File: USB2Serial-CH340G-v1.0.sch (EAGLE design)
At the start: 23 parts, among them CN2 47346-0001, IC2 AMS1117-3.3, Q1 12MHz, U1 CH340G

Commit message: Fix some names
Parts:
- CN1: value (none) -> UART
- renumbered IC2 to IC1, J1 to CN1
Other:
- note added: "(c) Andriy Golovnya"
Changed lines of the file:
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@@
 <part name="C5" library="rcl" library_urn="urn:adsk.eagle:library:334" deviceset="C-EU" device="C0402" package3d_urn="urn:adsk.eagle:package:23626/2" value="100nF"/>
 <part name="C6" library="rcl" library_urn="urn:adsk.eagle:library:334" deviceset="C-EU" device="C0402" package3d_urn="urn:adsk.eagle:package:23626/2" value="100nF"/>
-<part name="IC2" library="v-reg" library_urn="urn:adsk.eagle:library:409" deviceset="LD117A?*" device="S" package3d_urn="urn:adsk.eagle:package:30370/1" technology="33TR" value="AMS1117-3.3"/>
+<part name="IC1" library="v-reg" library_urn="urn:adsk.eagle:library:409" deviceset="LD117A?*" device="S" package3d_urn="urn:adsk.eagle:package:30370/1" technology="33TR" value="AMS1117-3.3"/>
 <part name="SUPPLY2" library="SparkFun-PowerSymbols" library_urn="urn:adsk.eagle:library:530" deviceset="5V" device=""/>
 <part name="SUPPLY3" library="SparkFun-PowerSymbols" library_urn="urn:adsk.eagle:library:530" deviceset="3.3V" device=""/>
@@
 <part name="GND5" library="SparkFun-PowerSymbols" library_urn="urn:adsk.eagle:library:530" deviceset="GND" device=""/>
 <part name="FRAME1" library="frames" library_urn="urn:adsk.eagle:library:229" deviceset="DINA4_L" device=""/>
-<part name="J1" library="SparkFun-Connectors" library_urn="urn:adsk.eagle:library:513" deviceset="CONN_06" device="NO_SILK_FEMALE_PTH" package3d_urn="urn:adsk.eagle:package:38130/1"/>
+<part name="CN1" library="SparkFun-Connectors" library_urn="urn:adsk.eagle:library:513" deviceset="CONN_06" device="NO_SILK_FEMALE_PTH" package3d_urn="urn:adsk.eagle:package:38130/1" value="UART"/>
 <part name="GND1" library="SparkFun-PowerSymbols" library_urn="urn:adsk.eagle:library:530" deviceset="GND" device=""/>
 <part name="SUPPLY1" library="SparkFun-PowerSymbols" library_urn="urn:adsk.eagle:library:530" deviceset="5V" device=""/>
@@
 <text x="111.76" y="144.78" size="2.54" layer="94">3.3V generation</text>
 <text x="40.64" y="144.78" size="2.54" layer="94">LED indicators</text>
-<text x="177.8" y="144.78" size="2.54" layer="94">UART connector and VCC selection</text>
+<text x="175.26" y="144.78" size="2.54" layer="94">UART connector and VCC selection</text>
+<text x="165.1" y="27.94" size="2.54" layer="94">(c) Andriy Golovnya</text>
 </plain>
 <instances>
@@
 <attribute name="VALUE" x="138.684" y="117.221" size="1.778" layer="96"/>
 </instance>
-<instance part="IC2" gate="G$1" x="119.38" y="129.54" smashed="yes">
+<instance part="IC1" gate="G$1" x="119.38" y="129.54" smashed="yes">
 <attribute name="NAME" x="111.76" y="134.62" size="1.778" layer="95"/>
 <attribute name="VALUE" x="119.38" y="134.62" size="1.778" layer="96"/>
@@
 <attribute name="DRAWING_NAME" x="180.34" y="19.05" size="2.54" layer="94"/>
 </instance>
-<instance part="J1" gate="G$1" x="218.44" y="121.92" smashed="yes" rot="R180">
-<attribute name="VALUE" x="223.52" y="131.826" size="1.778" layer="96" font="vector" rot="R180"/>
-<attribute name="NAME" x="223.52" y="111.252" size="1.778" layer="95" font="vector" rot="R180"/>
+<instance part="CN1" gate="G$1" x="218.44" y="121.92" smashed="yes" rot="R180">
+<attribute name="VALUE" x="218.44" y="106.934" size="1.778" layer="96"/>
+<attribute name="NAME" x="218.44" y="109.728" size="1.778" layer="95"/>
 </instance>
 <instance part="GND1" gate="1" x="210.82" y="111.76" smashed="yes">
@@
 </instance>
 <instance part="SJ1" gate="G$1" x="187.96" y="129.54" smashed="yes" rot="R90">
-<attribute name="NAME" x="187.579" y="132.08" size="1.778" layer="95" rot="R90"/>
+<attribute name="NAME" x="185.42" y="132.461" size="1.778" layer="95"/>
 <attribute name="VALUE" x="189.865" y="132.08" size="1.778" layer="96" rot="R90"/>
 </instance>
@@
 <attribute name="VALUE" x="170.18" y="73.406" size="1.778" layer="96"/>
 </instance>
-<instance part="SUPPLY4" gate="G$1" x="187.96" y="83.82" smashed="yes">
-<attribute name="VALUE" x="185.42" y="86.614" size="1.778" layer="96"/>
+<instance part="SUPPLY4" gate="G$1" x="187.96" y="81.28" smashed="yes">
+<attribute name="VALUE" x="185.42" y="84.074" size="1.778" layer="96"/>
 </instance>
 <instance part="GND4" gate="1" x="119.38" y="111.76" smashed="yes">
@@
 <pinref part="C5" gate="G$1" pin="2"/>
 <pinref part="C6" gate="G$1" pin="2"/>
-<pinref part="IC2" gate="G$1" pin="ADJ"/>
+<pinref part="IC1" gate="G$1" pin="ADJ"/>
 <pinref part="GND4" gate="1" pin="GND"/>
 </segment>
@@
 </segment>
 <segment>
-<pinref part="J1" gate="G$1" pin="6"/>
+<pinref part="CN1" gate="G$1" pin="6"/>
 <wire x1="213.36" y1="114.3" x2="210.82" y2="114.3" width="0.1524" layer="91"/>
 <pinref part="GND1" gate="1" pin="GND"/>
@@
 <wire x1="109.22" y1="134.62" x2="109.22" y2="129.54" width="0.1524" layer="91"/>
 <pinref part="C5" gate="G$1" pin="1"/>
-<pinref part="IC2" gate="G$1" pin="IN"/>
+<pinref part="IC1" gate="G$1" pin="IN"/>
 <pinref part="SUPPLY2" gate="G$1" pin="5V"/>
 </segment>
@@
 <pinref part="C3" gate="G$1" pin="1"/>
 <pinref part="C6" gate="G$1" pin="1"/>
-<pinref part="IC2" gate="G$1" pin="OUT"/>
+<pinref part="IC1" gate="G$1" pin="OUT"/>
 <pinref part="SUPPLY3" gate="G$1" pin="3.3V"/>
 </segment>
@@
 <net name="UART_DTR" class="0">
 <segment>
-<pinref part="J1" gate="G$1" pin="1"/>
+<pinref part="CN1" gate="G$1" pin="1"/>
 <wire x1="213.36" y1="127" x2="205.74" y2="127" width="0.1524" layer="91"/>
 <label x="200.66" y="127" size="1.778" layer="95"/>
@@
 <net name="UART_RX" class="0">
 <segment>
-<pinref part="J1" gate="G$1" pin="2"/>
+<pinref part="CN1" gate="G$1" pin="2"/>
 <wire x1="213.36" y1="124.46" x2="205.74" y2="124.46" width="0.1524" layer="91"/>
 <label x="200.66" y="124.46" size="1.778" layer="95"/>
@@
 <net name="UART_TX" class="0">
 <segment>
-<pinref part="J1" gate="G$1" pin="3"/>
+<pinref part="CN1" gate="G$1" pin="3"/>
 <wire x1="213.36" y1="121.92" x2="205.74" y2="121.92" width="0.1524" layer="91"/>
 <label x="200.66" y="121.92" size="1.778" layer="95"/>
@@
 <net name="UART_CTS" class="0">
 <segment>
-<pinref part="J1" gate="G$1" pin="5"/>
+<pinref part="CN1" gate="G$1" pin="5"/>
 <wire x1="213.36" y1="116.84" x2="205.74" y2="116.84" width="0.1524" layer="91"/>
 <label x="200.66" y="116.84" size="1.778" layer="95"/>
@@
 <net name="VCC" class="0">
 <segment>
-<pinref part="J1" gate="G$1" pin="4"/>
+<pinref part="CN1" gate="G$1" pin="4"/>
 <wire x1="213.36" y1="119.38" x2="187.96" y2="119.38" width="0.1524" layer="91"/>
 <wire x1="187.96" y1="119.38" x2="187.96" y2="124.46" width="0.1524" layer="91"/>
@@
 <segment>
 <wire x1="190.5" y1="81.28" x2="187.96" y2="81.28" width="0.1524" layer="91"/>
-<wire x1="187.96" y1="81.28" x2="187.96" y2="83.82" width="0.1524" layer="91"/>
 <pinref part="U1" gate="U1" pin="VCC"/>
 <pinref part="SUPPLY4" gate="G$1" pin="VCC"/>

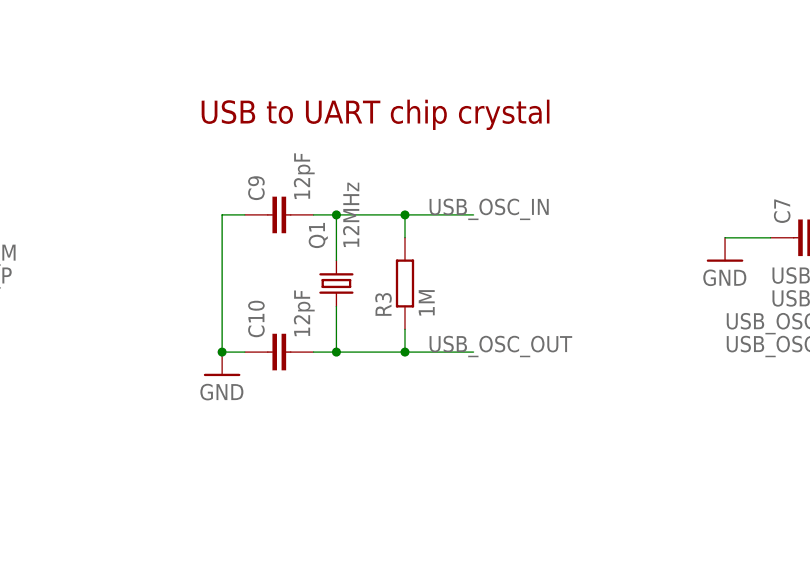
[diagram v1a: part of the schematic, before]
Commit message: Add basic board design. Remove R3 as not strictly needed.
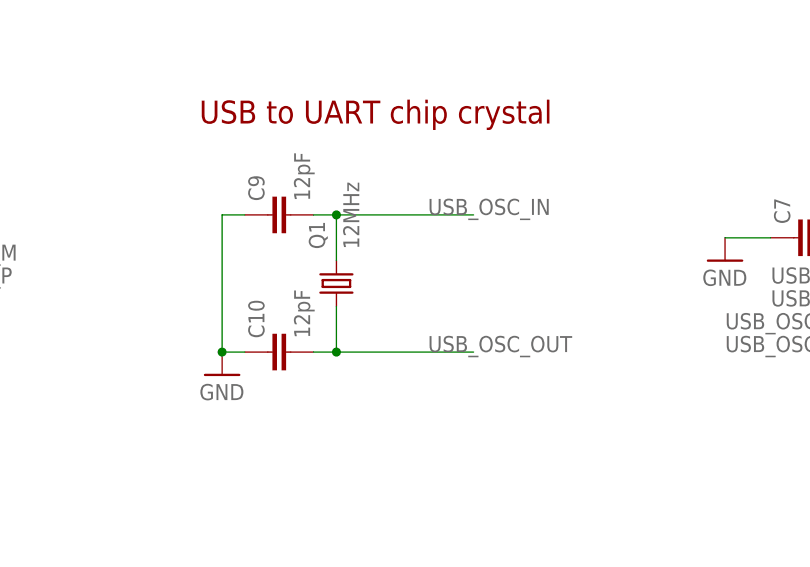
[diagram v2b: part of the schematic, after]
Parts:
- removed R3: 1M, rcl:R-EU_R0402
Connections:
- net USB_OSC_IN: no longer R3.2
- net USB_OSC_OUT: no longer R3.1
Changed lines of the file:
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@@
 <part name="C7" library="rcl" library_urn="urn:adsk.eagle:library:334" deviceset="C-EU" device="C0402" package3d_urn="urn:adsk.eagle:package:23626/2" value="100nF"/>
 <part name="Q1" library="crystal-geyer_V1_0" library_urn="urn:adsk.eagle:library:203" deviceset="KX" device="-7" package3d_urn="urn:adsk.eagle:package:11924/1" value="12MHz"/>
-<part name="R3" library="rcl" library_urn="urn:adsk.eagle:library:334" deviceset="R-EU_" device="R0402" package3d_urn="urn:adsk.eagle:package:23547/3" value="1M"/>
 <part name="C9" library="rcl" library_urn="urn:adsk.eagle:library:334" deviceset="C-EU" device="C0402" package3d_urn="urn:adsk.eagle:package:23626/2" value="12pF"/>
 <part name="C10" library="rcl" library_urn="urn:adsk.eagle:library:334" deviceset="C-EU" device="C0402" package3d_urn="urn:adsk.eagle:package:23626/2" value="12pF"/>
@@
 <attribute name="VALUE" x="132.08" y="77.47" size="1.778" layer="96" rot="R90"/>
 </instance>
-<instance part="R3" gate="G$1" x="137.16" y="73.66" smashed="yes" rot="R90">
-<attribute name="NAME" x="135.6614" y="69.85" size="1.778" layer="95" rot="R90"/>
-<attribute name="VALUE" x="140.462" y="69.85" size="1.778" layer="96" rot="R90"/>
-</instance>
 <instance part="C9" gate="G$1" x="121.92" y="81.28" smashed="yes" rot="R90">
 <attribute name="NAME" x="121.539" y="82.804" size="1.778" layer="95" rot="R90"/>
@@
 <segment>
 <wire x1="129.54" y1="76.2" x2="129.54" y2="81.28" width="0.1524" layer="91"/>
-<wire x1="129.54" y1="81.28" x2="137.16" y2="81.28" width="0.1524" layer="91"/>
-<wire x1="137.16" y1="81.28" x2="144.78" y2="81.28" width="0.1524" layer="91"/>
-<wire x1="137.16" y1="78.74" x2="137.16" y2="81.28" width="0.1524" layer="91"/>
-<junction x="137.16" y="81.28"/>
+<wire x1="129.54" y1="81.28" x2="144.78" y2="81.28" width="0.1524" layer="91"/>
 <wire x1="129.54" y1="81.28" x2="127" y2="81.28" width="0.1524" layer="91"/>
 <junction x="129.54" y="81.28"/>
 <label x="139.7" y="81.28" size="1.778" layer="95"/>
 <pinref part="Q1" gate="G$1" pin="2"/>
-<pinref part="R3" gate="G$1" pin="2"/>
 <pinref part="C9" gate="G$1" pin="2"/>
 </segment>
@@
 <segment>
 <wire x1="129.54" y1="71.12" x2="129.54" y2="66.04" width="0.1524" layer="91"/>
-<wire x1="129.54" y1="66.04" x2="137.16" y2="66.04" width="0.1524" layer="91"/>
-<wire x1="137.16" y1="66.04" x2="144.78" y2="66.04" width="0.1524" layer="91"/>
-<wire x1="137.16" y1="68.58" x2="137.16" y2="66.04" width="0.1524" layer="91"/>
-<junction x="137.16" y="66.04"/>
+<wire x1="129.54" y1="66.04" x2="144.78" y2="66.04" width="0.1524" layer="91"/>
 <wire x1="129.54" y1="66.04" x2="127" y2="66.04" width="0.1524" layer="91"/>
 <junction x="129.54" y="66.04"/>
 <label x="139.7" y="66.04" size="1.778" layer="95"/>
 <pinref part="Q1" gate="G$1" pin="1"/>
-<pinref part="R3" gate="G$1" pin="1"/>
 <pinref part="C10" gate="G$1" pin="2"/>
 </segment>
@@
 </sheet>
 </sheets>
+<errors>
+</errors>
 </schematic>
 </drawing>

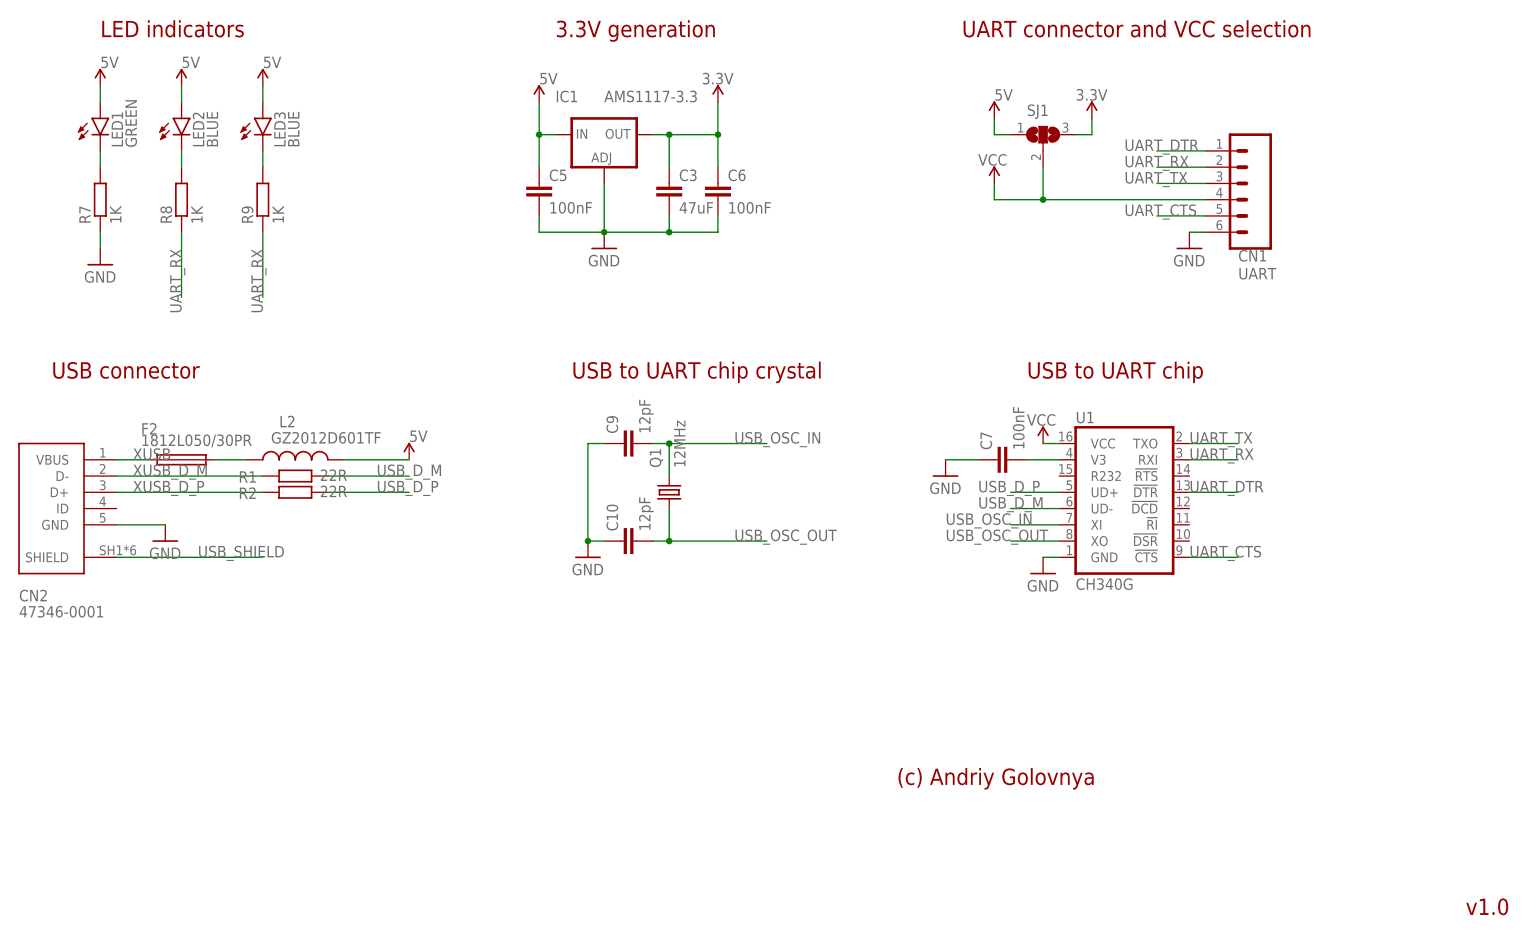
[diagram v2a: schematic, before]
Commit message: Route the board. Add texts and logos
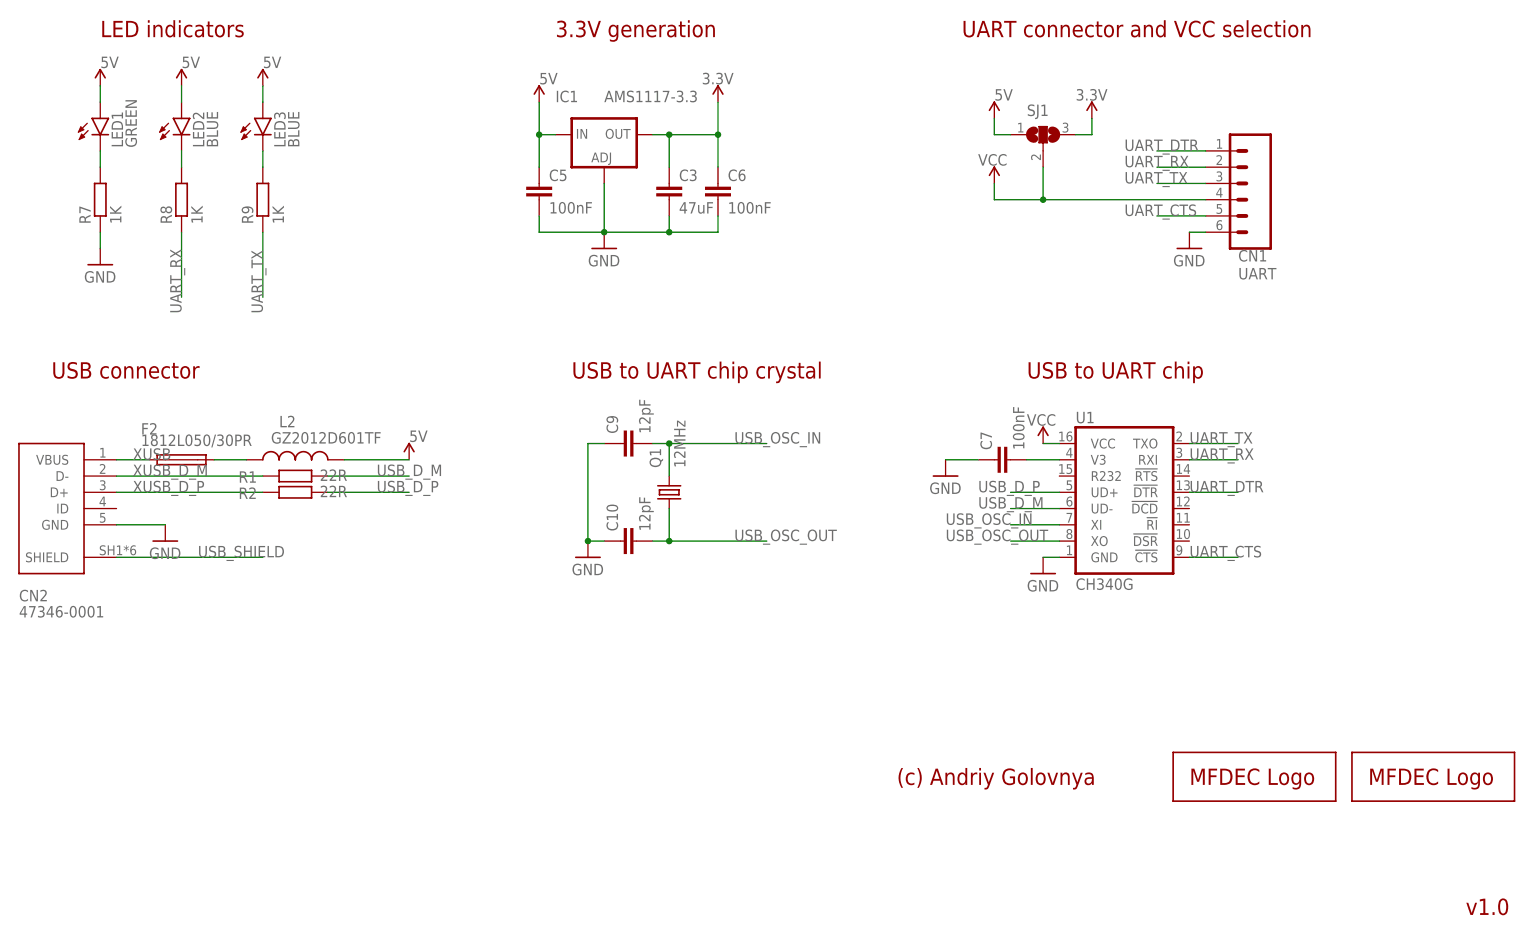
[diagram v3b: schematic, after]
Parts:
- added LOGO1: MFDECLOGO_L_20MM, _my_logos:MFDECLOGO_L_20MM
- added LOGO2: MFDECLOGO_SQ_10MM, _my_logos:MFDECLOGO_SQ_10MM
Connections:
- net UART_RX: no longer R9.1
- net UART_TX: now also R9.1
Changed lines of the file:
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@@
 <part name="LED3" library="led" library_urn="urn:adsk.eagle:library:259" deviceset="LED" device="SML0603" package3d_urn="urn:adsk.eagle:package:15832/1" value="BLUE"/>
 <part name="R9" library="rcl" library_urn="urn:adsk.eagle:library:334" deviceset="R-EU_" device="R0402" package3d_urn="urn:adsk.eagle:package:23547/3" value="1K"/>
+<part name="LOGO1" library="_my_logos" deviceset="MFDECLOGO" device="_L_20MM" value="MFDECLOGO_L_20MM"/>
+<part name="LOGO2" library="_my_logos" deviceset="MFDECLOGO" device="_SQ_10MM"/>
 </parts>
 <sheets>
@@
 <attribute name="VALUE" x="69.342" y="115.57" size="1.778" layer="96" rot="R90"/>
 </instance>
+<instance part="LOGO1" gate="G$1" x="236.22" y="25.4" smashed="yes"/>
+<instance part="LOGO2" gate="G$1" x="208.28" y="25.4" smashed="yes"/>
 </instances>
 <busses>
@@
 <label x="53.34" y="101.6" size="1.778" layer="95" rot="R90"/>
 </segment>
+</net>
+<net name="UART_TX" class="0">
+<segment>
+<pinref part="CN1" gate="G$1" pin="3"/>
+<wire x1="213.36" y1="121.92" x2="205.74" y2="121.92" width="0.1524" layer="91"/>
+<label x="200.66" y="121.92" size="1.778" layer="95"/>
+</segment>
+<segment>
+<pinref part="U1" gate="U1" pin="TXO"/>
+<wire x1="210.82" y1="81.28" x2="218.44" y2="81.28" width="0.1524" layer="91"/>
+<label x="210.82" y="81.28" size="1.778" layer="95"/>
+</segment>
 <segment>
 <pinref part="R9" gate="G$1" pin="1"/>
@@
 </segment>
 </net>
-<net name="UART_TX" class="0">
-<segment>
-<pinref part="CN1" gate="G$1" pin="3"/>
-<wire x1="213.36" y1="121.92" x2="205.74" y2="121.92" width="0.1524" layer="91"/>
-<label x="200.66" y="121.92" size="1.778" layer="95"/>
-</segment>
-<segment>
-<pinref part="U1" gate="U1" pin="TXO"/>
-<wire x1="210.82" y1="81.28" x2="218.44" y2="81.28" width="0.1524" layer="91"/>
-<label x="210.82" y="81.28" size="1.778" layer="95"/>
-</segment>
-</net>
